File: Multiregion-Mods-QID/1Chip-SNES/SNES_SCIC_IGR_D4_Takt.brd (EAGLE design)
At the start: 88.9 x 40.6 mm, 42 parts, among them IC1 74HC27D, IC2 74HC30D

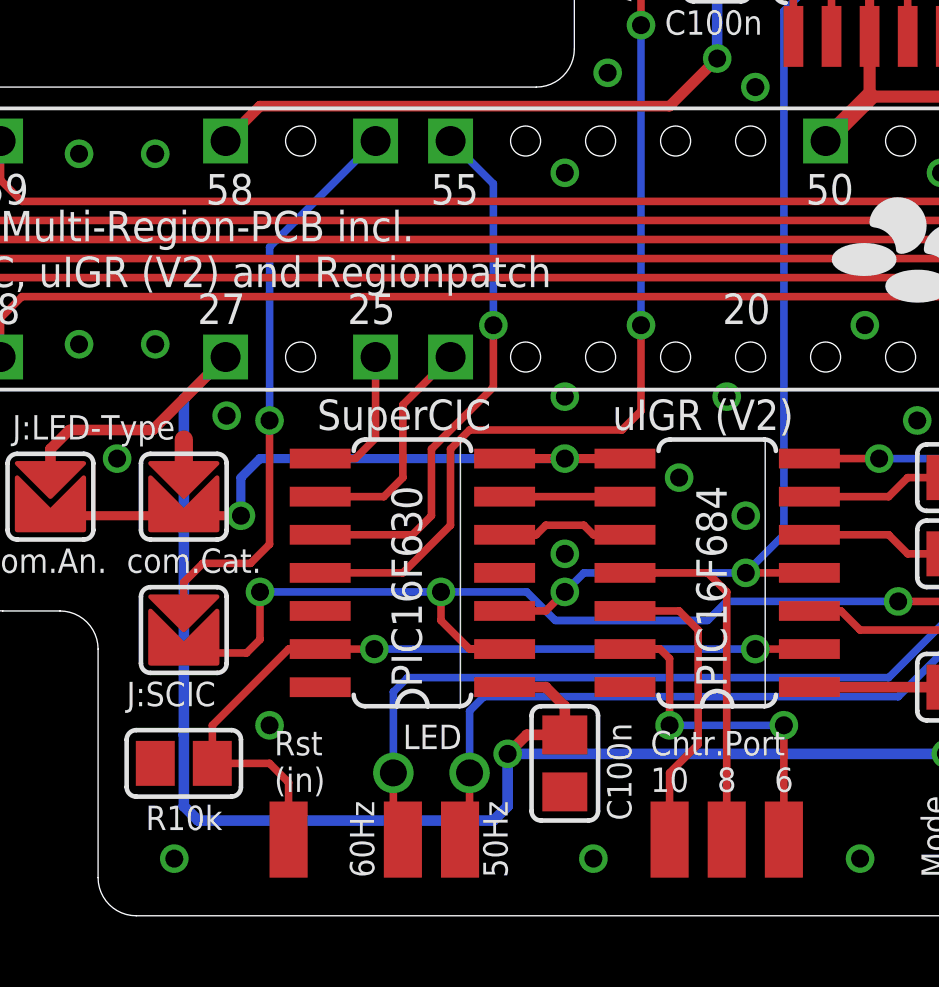
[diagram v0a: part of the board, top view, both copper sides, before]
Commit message: Minor Update (routing of wires from SuperCIC to cart.slot)
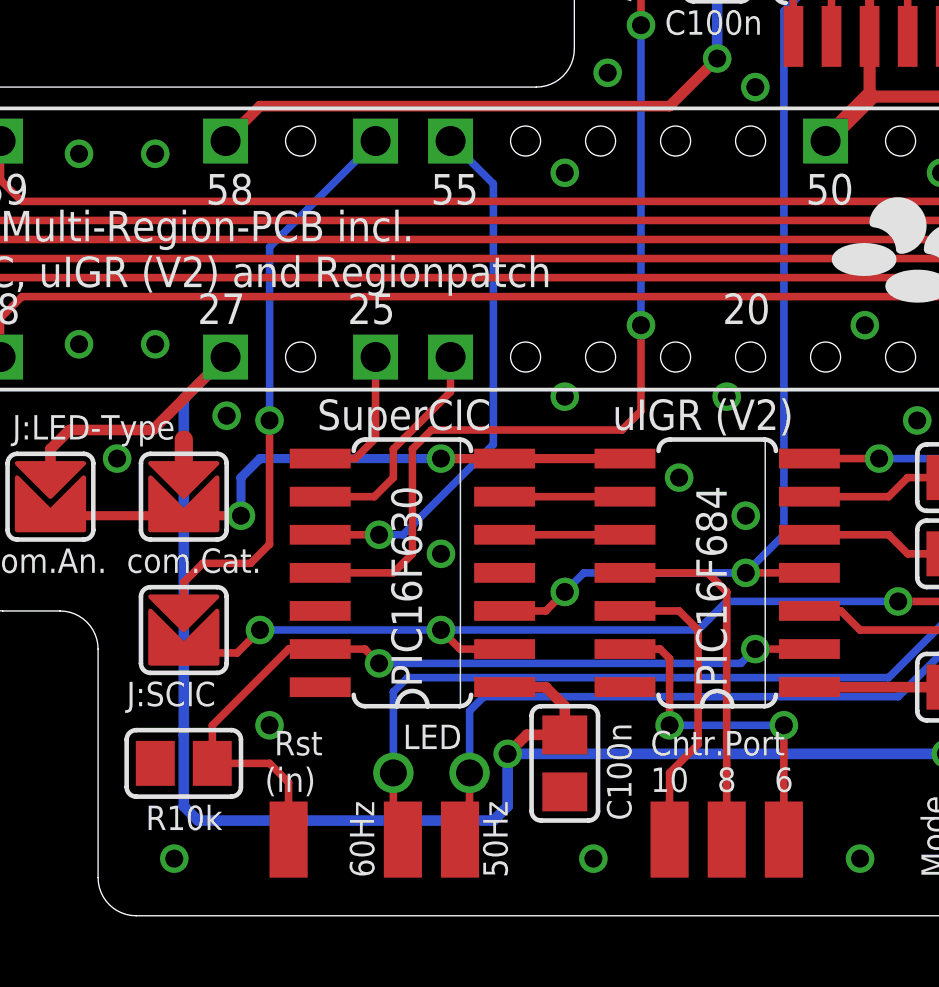
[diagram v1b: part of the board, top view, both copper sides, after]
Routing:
- net N$39: track 43.6 -> 40.8 mm
- net N$3: track 32.8 -> 33.4 mm
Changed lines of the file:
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@@
 <?xml version="1.0" encoding="utf-8"?>
 <!DOCTYPE eagle SYSTEM "eagle.dtd">
-<eagle version="6.4">
+<eagle version="7.2.0">
 <drawing>
 <settings>
@@
 <setting verticaltext="up"/>
 </settings>
-<grid distance="0.05" unitdist="inch" unit="mm" style="lines" multiple="1" display="yes" altdistance="0.00625" altunitdist="inch" altunit="inch"/>
+<grid distance="0.05" unitdist="inch" unit="inch" style="lines" multiple="1" display="yes" altdistance="0.00625" altunitdist="inch" altunit="inch"/>
 <layers>
 <layer number="1" name="Top" color="4" fill="1" visible="yes" active="yes"/>
@@
 <text x="23.1775" y="6.985" size="0.8128" layer="25" font="vector" ratio="15" rot="R90">60Hz</text>
 <text x="46.0375" y="17.145" size="0.8128" layer="25" font="vector" ratio="15" rot="R90">2xR220</text>
-<text x="19.84375" y="9.8425" size="0.8128" layer="25" font="vector" ratio="15">Rst
+<text x="19.52625" y="9.8425" size="0.8128" layer="25" font="vector" ratio="15"> Rst
 (in)</text>
 <text x="32.86125" y="36.195" size="0.8128" layer="25" font="vector" ratio="15" rot="R90">/Rst
@@
 <pass name="Default">
 <param name="RoutingGrid" value="50mil"/>
+<param name="AutoGrid" value="1"/>
+<param name="Efforts" value="0"/>
+<param name="TopRouterVariant" value="1"/>
 <param name="tpViaShape" value="round"/>
 <param name="PrefDir.1" value="|"/>
@@
 <contactref element="C9" pad="2"/>
 <contactref element="C1" pad="2"/>
-<via x="29.5275" y="17.78" extent="1-16" drill="0.6"/>
+<via x="25.4" y="17.78" extent="1-16" drill="0.6"/>
 <via x="79.375" y="28.575" extent="1-16" drill="0.6"/>
 <via x="74.295" y="28.575" extent="1-16" drill="0.6"/>
@@
 <contactref element="CTRL1" pad="1"/>
 <contactref element="U$1" pad="P$2"/>
-<wire x1="27.5209" y1="14.605" x2="26.3525" y2="14.605" width="0.254" layer="1"/>
-<wire x1="26.3525" y1="14.605" x2="25.4" y2="15.5575" width="0.254" layer="1"/>
-<via x="25.4" y="16.51" extent="1-16" drill="0.6"/>
-<wire x1="25.4" y1="16.51" x2="19.3675" y2="16.51" width="0.254" layer="16"/>
-<wire x1="16.8275" y1="14.474825" x2="18.919825" y2="14.474825" width="0.254" layer="1"/>
-<wire x1="18.919825" y1="14.474825" x2="19.3675" y2="14.9225" width="0.254" layer="1"/>
-<wire x1="19.3675" y1="14.9225" x2="19.3675" y2="16.51" width="0.254" layer="1"/>
-<via x="19.3675" y="16.51" extent="1-16" drill="0.6"/>
-<wire x1="25.4" y1="16.51" x2="28.2575" y2="16.51" width="0.254" layer="16"/>
-<wire x1="28.2575" y1="16.51" x2="29.21" y2="15.5575" width="0.254" layer="16"/>
-<wire x1="29.21" y1="15.5575" x2="34.29" y2="15.5575" width="0.254" layer="16"/>
-<wire x1="34.29" y1="15.5575" x2="34.925" y2="16.1925" width="0.254" layer="16"/>
+<wire x1="27.5209" y1="14.605" x2="26.035" y2="14.605" width="0.254" layer="1"/>
+<via x="25.4" y="15.24" extent="1-16" drill="0.6"/>
+<wire x1="25.4" y1="15.24" x2="19.3675" y2="15.24" width="0.254" layer="16"/>
+<wire x1="16.8275" y1="14.474825" x2="18.602325" y2="14.474825" width="0.254" layer="1"/>
+<wire x1="18.602325" y1="14.474825" x2="19.3675" y2="15.24" width="0.254" layer="1"/>
+<via x="19.3675" y="15.24" extent="1-16" drill="0.6"/>
+<wire x1="25.4" y1="15.24" x2="33.9725" y2="15.24" width="0.254" layer="16"/>
+<wire x1="33.9725" y1="15.24" x2="34.925" y2="16.1925" width="0.254" layer="16"/>
 <wire x1="34.925" y1="16.1925" x2="40.64" y2="16.1925" width="0.254" layer="16"/>
 <via x="40.64" y="16.1925" extent="1-16" drill="0.6"/>
@@
 <wire x1="46.355" y1="16.1925" x2="46.99" y2="15.5575" width="0.254" layer="1"/>
 <wire x1="46.99" y1="15.5575" x2="46.99" y2="8.255" width="0.254" layer="1"/>
-<wire x1="25.4" y1="15.5575" x2="25.4" y2="16.51" width="0.254" layer="1"/>
+<wire x1="26.035" y1="14.605" x2="25.4" y2="15.24" width="0.254" layer="1"/>
 </signal>
 <signal name="N$48">
 <contactref element="U$2" pad="10"/>
-<wire x1="21.3741" y1="18.415" x2="24.4475" y2="18.415" width="0.254" layer="1"/>
-<wire x1="24.4475" y1="18.415" x2="25.0825" y2="19.05" width="0.254" layer="1"/>
 <contactref element="U$6" pad="55"/>
-<wire x1="25.0825" y1="19.05" x2="25.0825" y2="21.2725" width="0.254" layer="1"/>
-<via x="27.14625" y="25.4" extent="1-16" drill="0.6"/>
-<wire x1="27.14625" y1="25.4" x2="27.14625" y2="30.11375" width="0.254" layer="16"/>
+<wire x1="27.14625" y1="21.43125" x2="27.14625" y2="30.11375" width="0.254" layer="16"/>
 <wire x1="27.14625" y1="30.11375" x2="25.72" y2="31.54" width="0.254" layer="16"/>
-<wire x1="25.0825" y1="21.2725" x2="27.14625" y2="23.33625" width="0.254" layer="1"/>
-<wire x1="27.14625" y1="23.33625" x2="27.14625" y2="25.4" width="0.254" layer="1"/>
+<wire x1="21.3741" y1="18.415" x2="23.33625" y2="18.415" width="0.254" layer="1"/>
+<via x="23.33625" y="18.415" extent="1-16" drill="0.6"/>
+<wire x1="23.33625" y1="18.415" x2="24.13" y2="18.415" width="0.254" layer="16"/>
+<wire x1="24.13" y1="18.415" x2="27.14625" y2="21.43125" width="0.254" layer="16"/>
 </signal>
 <signal name="N$49">
 <contactref element="U$2" pad="9"/>
-<wire x1="21.3741" y1="19.685" x2="23.495" y2="19.685" width="0.254" layer="1"/>
-<wire x1="23.495" y1="19.685" x2="24.13" y2="20.32" width="0.254" layer="1"/>
-<wire x1="24.13" y1="20.32" x2="24.13" y2="22.75" width="0.254" layer="1"/>
-<wire x1="24.13" y1="22.75" x2="25.72" y2="24.34" width="0.254" layer="1"/>
 <contactref element="U$6" pad="24"/>
+<wire x1="21.3741" y1="19.685" x2="23.1775" y2="19.685" width="0.254" layer="1"/>
+<wire x1="23.1775" y1="19.685" x2="23.8125" y2="20.32" width="0.254" layer="1"/>
+<wire x1="23.8125" y1="20.32" x2="23.8125" y2="21.2725" width="0.254" layer="1"/>
+<wire x1="23.8125" y1="21.2725" x2="25.7175" y2="23.1775" width="0.254" layer="1"/>
+<wire x1="25.7175" y1="23.1775" x2="25.7175" y2="24.3375" width="0.254" layer="1"/>
+<wire x1="25.7175" y1="24.3375" x2="25.72" y2="24.34" width="0.254" layer="1"/>
 </signal>
 <signal name="N$51">
@@
 <contactref element="U$2" pad="11"/>
 <contactref element="RES-OUT" pad="1"/>
-<wire x1="21.3741" y1="17.145" x2="24.13" y2="17.145" width="0.254" layer="1"/>
-<wire x1="24.13" y1="17.145" x2="25.7175" y2="18.7325" width="0.254" layer="1"/>
-<wire x1="25.7175" y1="18.7325" x2="25.7175" y2="21.2725" width="0.254" layer="1"/>
-<wire x1="25.7175" y1="21.2725" x2="26.3525" y2="21.9075" width="0.254" layer="1"/>
-<wire x1="26.3525" y1="21.9075" x2="31.4325" y2="21.9075" width="0.254" layer="1"/>
+<wire x1="25.0825" y1="21.9075" x2="31.4325" y2="21.9075" width="0.254" layer="1"/>
 <wire x1="32.0675" y1="22.5425" x2="31.4325" y2="21.9075" width="0.254" layer="1"/>
 <wire x1="32.0675" y1="22.5425" x2="32.0675" y2="25.4" width="0.254" layer="1"/>
@@
 <wire x1="31.75" y1="40.64" x2="32.0675" y2="40.64" width="0.254" layer="1"/>
 <wire x1="32.0675" y1="40.64" x2="32.0675" y2="35.40125" width="0.254" layer="1"/>
+<wire x1="25.0825" y1="21.9075" x2="24.4475" y2="21.2725" width="0.254" layer="1"/>
+<wire x1="24.4475" y1="21.2725" x2="24.4475" y2="17.78" width="0.254" layer="1"/>
+<wire x1="24.4475" y1="17.78" x2="23.8125" y2="17.145" width="0.254" layer="1"/>
+<wire x1="23.8125" y1="17.145" x2="21.3741" y2="17.145" width="0.254" layer="1"/>
 </signal>
 <signal name="N$10">
@@
 <contactref element="R1" pad="2"/>
 <contactref element="RES-IN" pad="1"/>
-<via x="23.1775" y="14.605" extent="1-16" drill="0.6"/>
-<wire x1="23.1775" y1="14.605" x2="35.8775" y2="14.605" width="0.254" layer="16"/>
+<via x="23.33625" y="14.12875" extent="1-16" drill="0.6"/>
 <via x="35.8775" y="14.605" extent="1-16" drill="0.6"/>
 <wire x1="21.3741" y1="14.605" x2="20.32" y2="14.605" width="0.254" layer="1"/>
@@
 <wire x1="19.685" y1="10.795" x2="20.32" y2="10.16" width="0.254" layer="1"/>
 <wire x1="20.32" y1="10.16" x2="20.32" y2="8.255" width="0.254" layer="1"/>
-<wire x1="21.3741" y1="14.605" x2="23.1775" y2="14.605" width="0.254" layer="1"/>
 <wire x1="35.8775" y1="14.605" x2="37.6809" y2="14.605" width="0.254" layer="1"/>
+<wire x1="21.3741" y1="14.605" x2="22.86" y2="14.605" width="0.254" layer="1"/>
+<wire x1="22.86" y1="14.605" x2="23.33625" y2="14.12875" width="0.254" layer="1"/>
+<wire x1="23.33625" y1="14.12875" x2="35.40125" y2="14.12875" width="0.254" layer="16"/>
+<wire x1="35.40125" y1="14.12875" x2="35.8775" y2="14.605" width="0.254" layer="16"/>
 </signal>
 <signal name="N$12">
@@
 <contactref element="U$3" pad="10"/>
 <contactref element="U$2" pad="5"/>
-<wire x1="27.5209" y1="18.415" x2="28.575" y2="18.415" width="0.254" layer="1"/>
-<wire x1="28.575" y1="18.415" x2="28.8925" y2="18.7325" width="0.254" layer="1"/>
-<wire x1="28.8925" y1="18.7325" x2="30.1625" y2="18.7325" width="0.254" layer="1"/>
-<wire x1="30.1625" y1="18.7325" x2="30.48" y2="18.415" width="0.254" layer="1"/>
-<wire x1="30.48" y1="18.415" x2="31.5341" y2="18.415" width="0.254" layer="1"/>
+<wire x1="27.5209" y1="18.415" x2="31.5341" y2="18.415" width="0.254" layer="1"/>
 </signal>
 <signal name="N$52">
@@
 <contactref element="U$2" pad="7"/>
 <contactref element="U$4" pad="P$2"/>
-<wire x1="27.5209" y1="20.955" x2="29.5275" y2="20.955" width="0.3048" layer="1"/>
-<wire x1="29.5275" y1="20.955" x2="31.5341" y2="20.955" width="0.3048" layer="1"/>
-<via x="29.5275" y="20.955" extent="1-16" drill="0.6"/>
+<wire x1="27.5209" y1="20.955" x2="25.4" y2="20.955" width="0.3048" layer="1"/>
+<wire x1="25.4" y1="20.955" x2="31.5341" y2="20.955" width="0.3048" layer="1"/>
+<via x="25.4" y="20.955" extent="1-16" drill="0.6"/>
 <contactref element="U$5" pad="P$2"/>
-<wire x1="19.3675" y1="20.955" x2="29.5275" y2="20.955" width="0.3048" layer="16"/>
+<wire x1="19.3675" y1="20.955" x2="25.4" y2="20.955" width="0.3048" layer="16"/>
 <wire x1="19.3675" y1="20.955" x2="18.7325" y2="20.32" width="0.3048" layer="16"/>
 <wire x1="16.8275" y1="18.919825" x2="17.014825" y2="18.919825" width="0.3048" layer="1"/>
